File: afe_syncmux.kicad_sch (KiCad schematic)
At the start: 21 parts, among them U22 THS7353

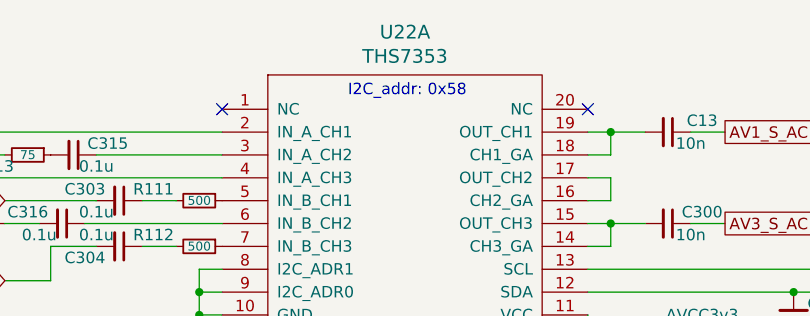
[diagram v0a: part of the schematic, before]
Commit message: update schematic to v1.5
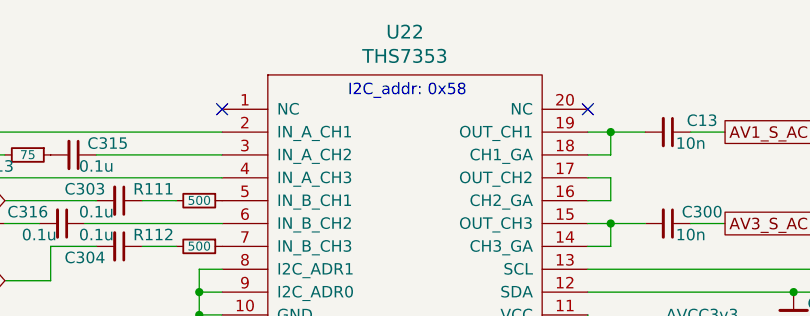
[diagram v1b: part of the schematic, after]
